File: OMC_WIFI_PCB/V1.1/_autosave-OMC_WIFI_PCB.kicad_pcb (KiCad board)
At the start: 2 copper layers, 103.2 x 83.1 mm, 18 parts, among them J1 ESP32_Left, J10 Control_ACS712, J11 Control_ZMPT101B, J2 ESP32_Right, J3 Power_In, J4 Switch, J5 Pins_FT232R, J6 Line_Relay, J7 Control_Relay, J8 Line_ACS712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

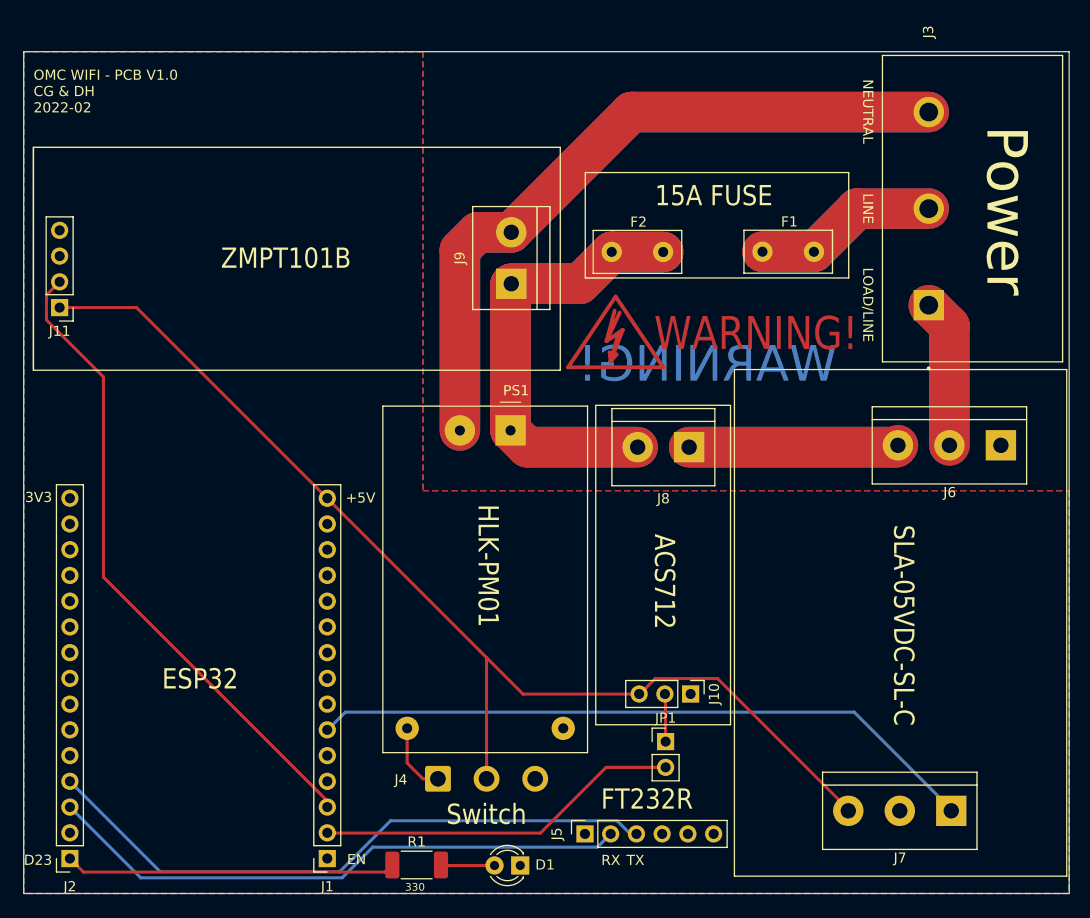
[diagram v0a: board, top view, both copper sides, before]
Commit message: Librerías para clavijas
+ Esquemático y footprint de clavija macho
+ Esquemático y footprint de clavija hembra
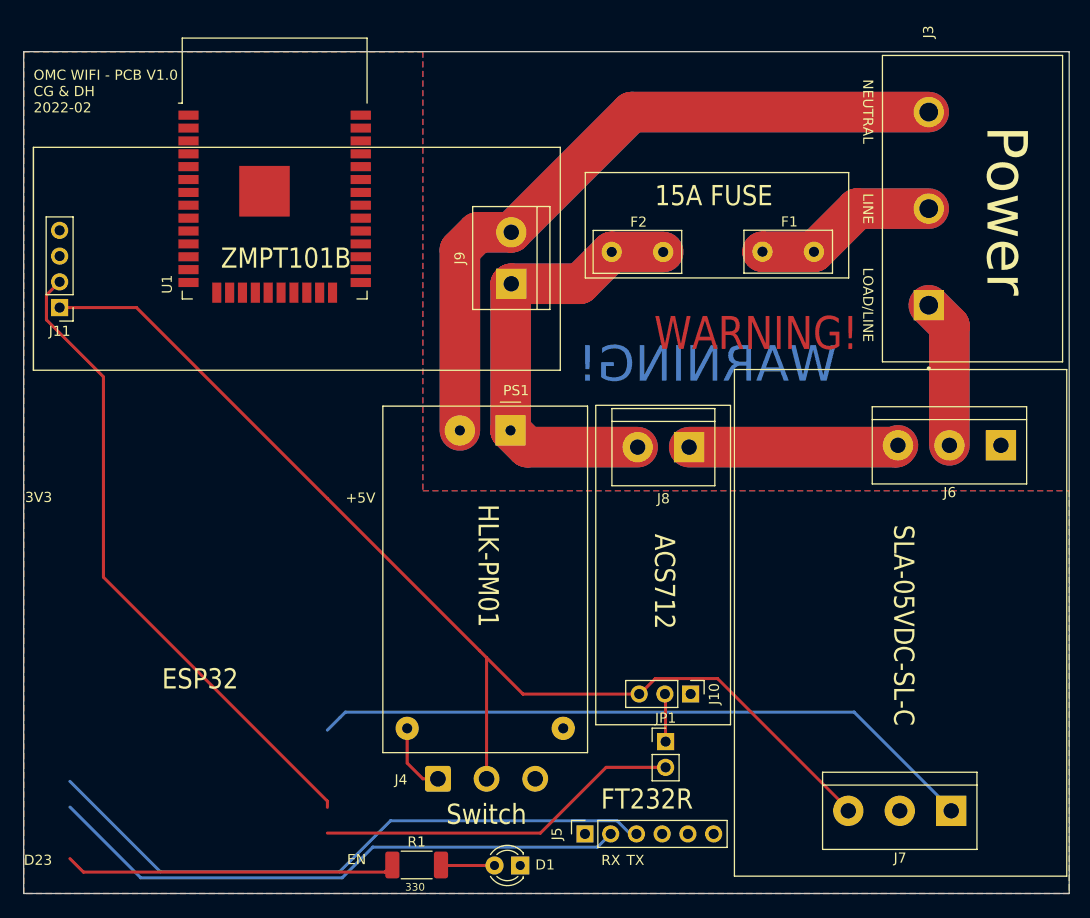
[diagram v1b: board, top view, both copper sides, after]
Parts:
- removed J1: ESP32_Left, Connector_PinSocket_2.54mm:PinSocket_1x15_P2.54mm_Vertical
- removed J2: ESP32_Right, Connector_PinSocket_2.54mm:PinSocket_1x15_P2.54mm_Vertical
- removed REF**: Symbol_HighVoltage_Type2_CopperTop_VerySmall, Symbol:Symbol_HighVoltage_Type2_CopperTop_VerySmall
- added U1: ESP32-WROOM-32, RF_Module:ESP32-WROOM-32, F.Cu at (601.3, -967.4)
